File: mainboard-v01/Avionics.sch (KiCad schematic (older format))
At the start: 35 parts, among them U1 MAX706R, U2 FXAS21002FXAS21002, U3 LSM9DS1, U4 ATSAMD21G-A, Y1 32.768kHz

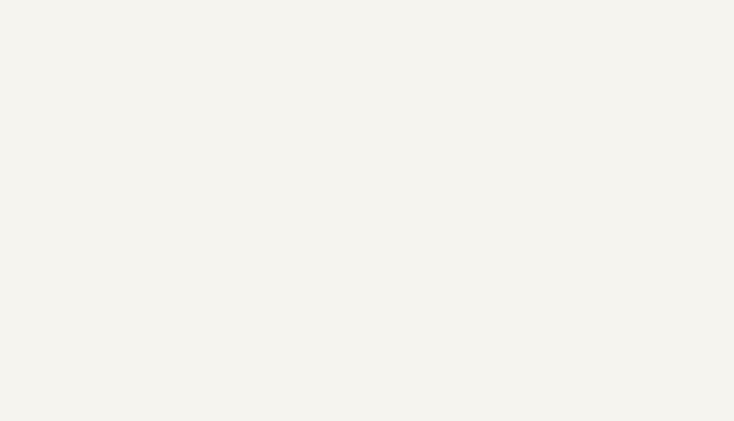
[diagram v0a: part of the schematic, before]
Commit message: adding v01 schematic pdf
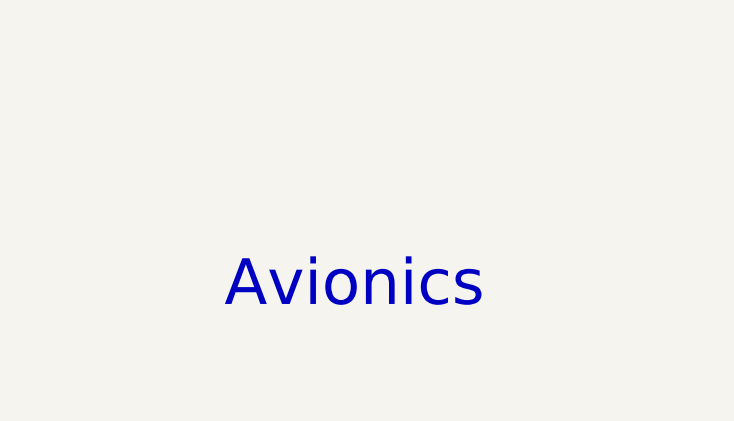
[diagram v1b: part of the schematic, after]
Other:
- note added: "Avionics"
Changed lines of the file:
@@
 Wire Notes Line
 	5700 700  5700 8000
+Text Notes 9200 7600 0    200  ~ 0
+Avionics
 $EndSCHEMATC
